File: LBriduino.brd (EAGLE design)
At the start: 45.4 x 27.9 mm, 13 parts, among them J1 105017-0001

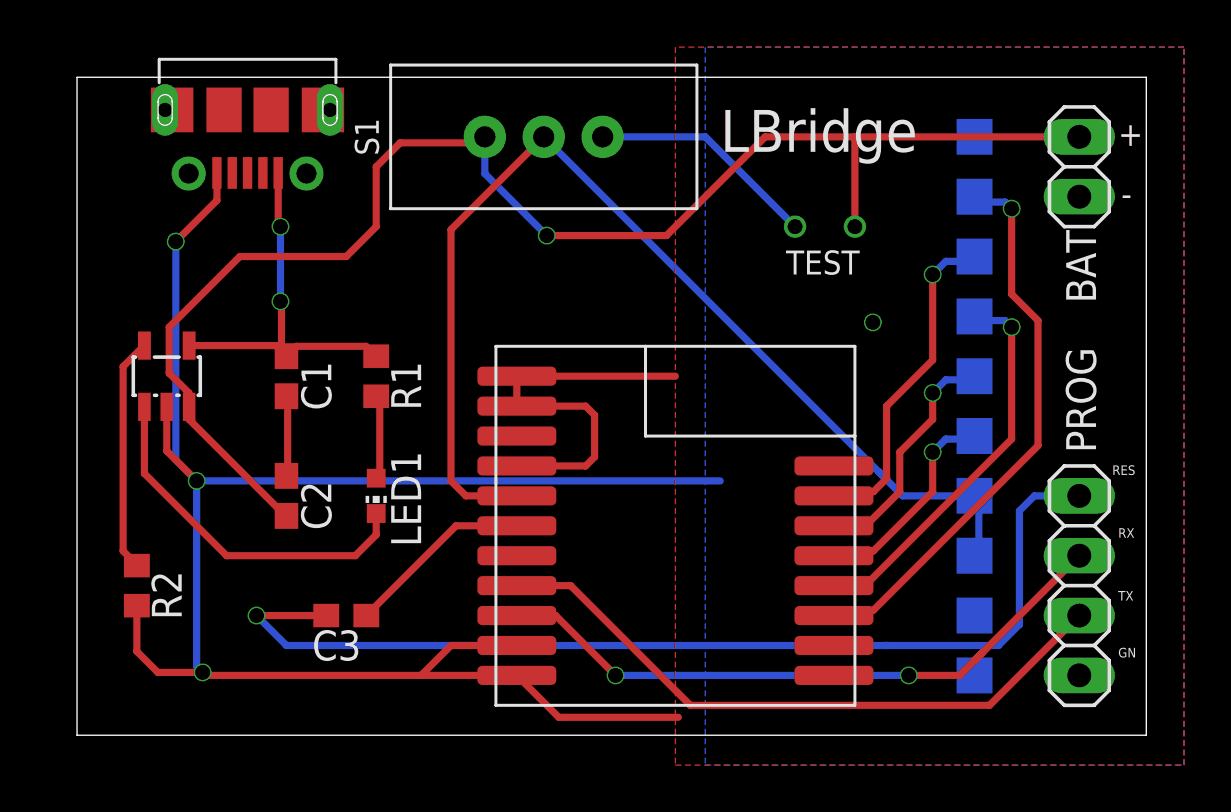
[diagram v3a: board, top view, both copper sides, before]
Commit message: redesign: missing ground bugfix, charging-IC-cooling, bluetooth-area copper-free
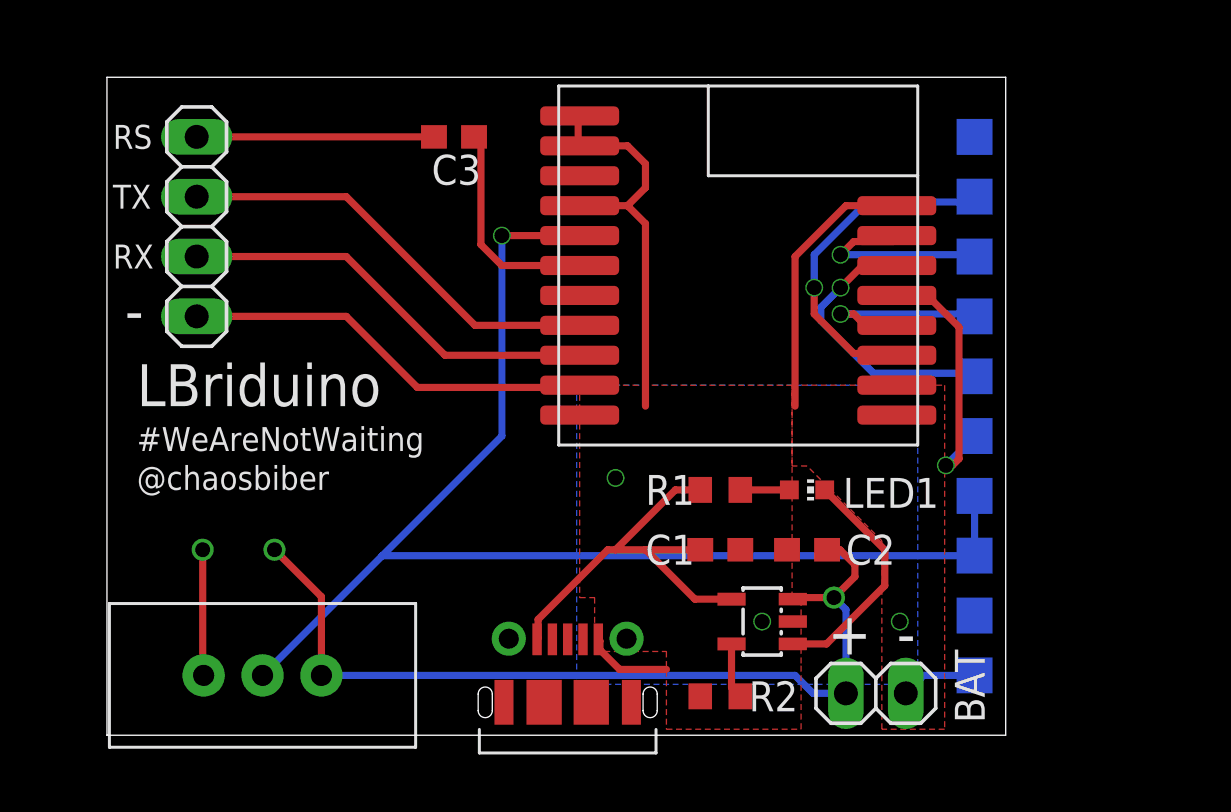
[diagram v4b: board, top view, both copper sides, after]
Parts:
- moved PROG 40.4 mm to (5.08, 21.6)
- moved J1 28.6 mm to (20.8, 1.40), turned to 0 degrees
- moved U$2 27.3 mm to (29.1, 4.83), turned to 90 degrees
- moved S1 25.8 mm to (7.87, 2.54), turned to 180 degrees
- moved R2 25.2 mm to (27.3, 1.65), turned to 180 degrees
- moved BAT 24.0 mm to (33.9, 1.78), turned to 180 degrees
- moved C2 22.2 mm to (31.0, 7.87), turned to 0 degrees
- moved C3 20.8 mm to (16.0, 25.4)
- moved C1 19.8 mm to (27.3, 7.87), turned to 0 degrees
- moved LED1 18.3 mm to (31.0, 10.4), turned to 270 degrees
- moved R1 15.4 mm to (27.3, 10.4), turned to 0 degrees
- moved U$1 11.4 mm to (28.1, 19.9)
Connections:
- removed net N$4: C1.2, C2.1
- net GND: now also C1.2, C2.1
- net P.RXD: now also PROG.2; no longer PROG.3
- net P.TXD: now also PROG.3; no longer PROG.2
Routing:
- net GND: track 95.7 -> 53.6 mm, vias 4 -> 3
- net N$3: track 44.0 -> 10.1 mm, vias 1 -> 0
- net VCC: track 61.8 -> 38.0 mm
- net IRQ: track 24.1 -> 14.6 mm
- net P.RXD: track 27.5 -> 18.0 mm, vias 2 -> 0
- net P.TXD: track 27.6 -> 18.5 mm
- net MISO: track 16.7 -> 8.34 mm
- net N$6: track 9.95 -> 2.38 mm
- net SS: track 14.3 -> 8.48 mm
- net N$2: track 15.6 -> 10.1 mm
- net SWITCH: track 48.5 -> 53.9 mm, vias 0 -> 1
- net TEST: track 9.75 -> 5.35 mm
- net N$4: track 3.40 -> 0.00 mm
- net SCK: track 9.18 -> 11.2 mm
- net +5V: track 16.2 -> 18.1 mm, vias 2 -> 0
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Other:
- board size 45.4 x 27.9 mm -> 38.2 x 27.9 mm
- board text added: "#WeAreNotWaiting"
- board text added: "@chaosbiber"
- board text added: "LBriduino"
- board text added: "RS"
- board text removed: "GN"
- board text removed: "LBridge"
- board text removed: "RES"
- board text removed: "TEST"

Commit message: made it smaller
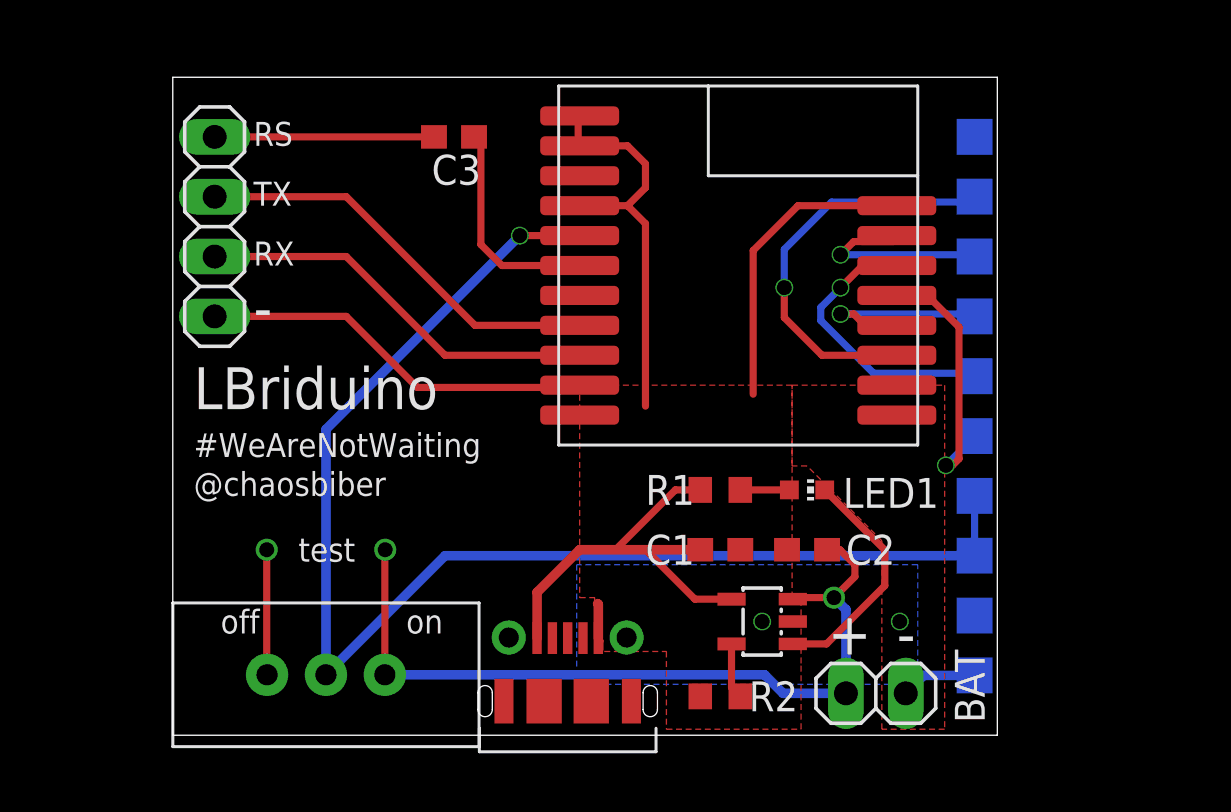
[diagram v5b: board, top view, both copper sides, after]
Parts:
- moved S1 2.69 mm to (10.6, 2.57)
- moved PROG 0.76 mm to (5.84, 21.6)
- moved J1 0.05 mm to (20.8, 1.45)
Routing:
- net +5V: track 18.1 -> 22.8 mm
- net VCC: track 38.0 -> 34.5 mm
- net IRQ: track 14.6 -> 17.6 mm
- net SWITCH: track 53.9 -> 56.8 mm
- net GND: track 53.6 -> 52.6 mm, vias 3 -> 2
- net P.TXD: track 18.5 -> 17.8 mm
- net P.RXD: track 18.0 -> 17.2 mm
- net N$3: track 10.1 -> 9.31 mm
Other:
- board size 38.2 x 27.9 mm -> 35 x 27.9 mm
- board text added: "off"
- board text added: "on"
- board text added: "test"
